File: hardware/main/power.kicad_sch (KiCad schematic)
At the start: 0 parts

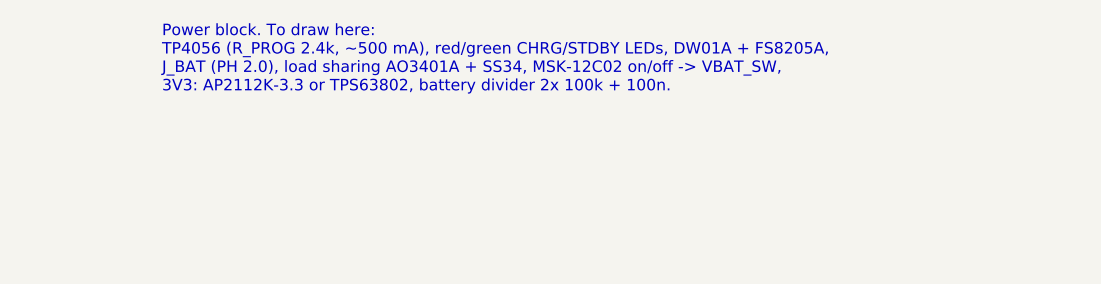
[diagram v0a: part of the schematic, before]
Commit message: hardware: footprints for every part, LCSC library, real A1S pin plan
- lib/lcsc: ESP32-A1S, NS4150B, FS8205A, MSK12C02, PJ-320D imported
  from LCSC with easyeda2kicad (3D paths fixed, NPTH pegs, A1S antenna
  keepout and courtyard), registered in all three projects.
- Parts table with footprint and LCSC number in hardware/README.md.
- The A1S keeps the codec's I2C/I2S inside: display moves to the
  ST7789's pins 14/13/15/22 (SPI or I2C), LED to 12, CHRG/STDBY to 4/2
  through BAT54W. J_SW and J_CHG for an off-board switch and charge LEDs.
- Block sheets use the module's real outputs (HPOUTL/R, SPOLP/N, SPORP/N).

Co-Authored-By: Claude Opus 5.5 <noreply@anthropic.com>
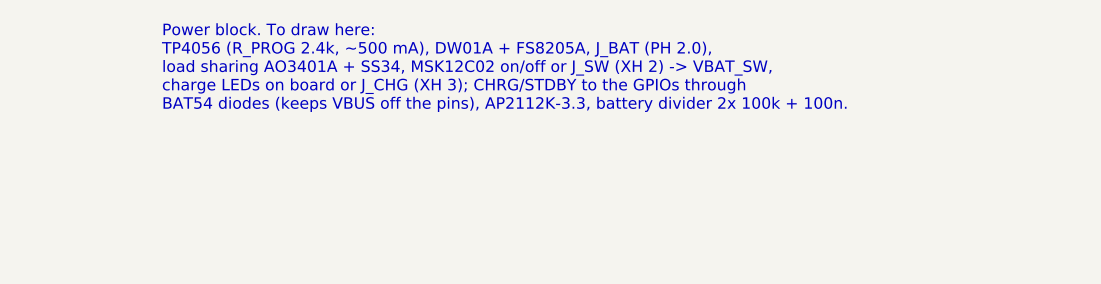
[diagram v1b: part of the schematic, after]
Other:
- note added: "Power block. To draw here: TP4056 (R_PROG 2.4k, ~500 mA), DW01A + FS8205A, J_BAT (PH 2.0), load sharing AO3401A + SS34, MSK12C02 on/off or J_SW (XH 2) -> VBAT_SW, charge LEDs on board or J_CHG (XH 3); CHRG/STDBY to the GPIOs through BAT54 diodes (keeps VBUS off the pins), AP2112K-3.3, battery divider 2x 100k + 100n."
- note removed: "Power block. To draw here: TP4056 (R_PROG 2.4k, ~500 mA), red/green CHRG/STDBY LEDs, DW01A + FS8205A, J_BAT (PH 2.0), load sharing AO3401A + SS34, MSK-12C02 on/off -> VBAT_SW, 3V3: AP2112K-3.3 or TPS63802, battery divider 2x 100k + 100n."
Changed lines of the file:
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@@
 		(rev "A")
 	)
-	(text "Power block. To draw here:\nTP4056 (R_PROG 2.4k, ~500 mA), red/green CHRG/STDBY LEDs, DW01A + FS8205A,\nJ_BAT (PH 2.0), load sharing AO3401A + SS34, MSK-12C02 on/off -> VBAT_SW,\n3V3: AP2112K-3.3 or TPS63802, battery divider 2x 100k + 100n."
+	(text "Power block. To draw here:\nTP4056 (R_PROG 2.4k, ~500 mA), DW01A + FS8205A, J_BAT (PH 2.0),\nload sharing AO3401A + SS34, MSK12C02 on/off or J_SW (XH 2) -> VBAT_SW,\ncharge LEDs on board or J_CHG (XH 3); CHRG/STDBY to the GPIOs through\nBAT54 diodes (keeps VBUS off the pins), AP2112K-3.3, battery divider 2x 100k + 100n."
 		(exclude_from_sim no)
 		(at 101.6 40.64 0)
@@
 		)
 	)
-	(hierarchical_label "CHRG"
+	(hierarchical_label "STDBY"
 		(shape output)
-		(at 50.8 55.88 180)
+		(at 50.8 60.96 180)
+		(effects
+			(font
+				(size 1.27 1.27)
+			)
+			(justify right)
+		)
+	)
+	(hierarchical_label "VBAT_SENSE"
+		(shape output)
+		(at 50.8 66.04 180)
 		(effects
 			(font
@@
 		)
 	)
-	(hierarchical_label "STDBY"
+	(hierarchical_label "CHRG"
 		(shape output)
-		(at 50.8 60.96 180)
+		(at 50.8 55.88 180)
 		(effects
 			(font
-				(size 1.27 1.27)
-			)
-			(justify right)
-		)
-	)
-	(hierarchical_label "VBAT_SENSE"
-		(shape output)
-		(at 50.8 66.04 180)
-		(effects
-			(font

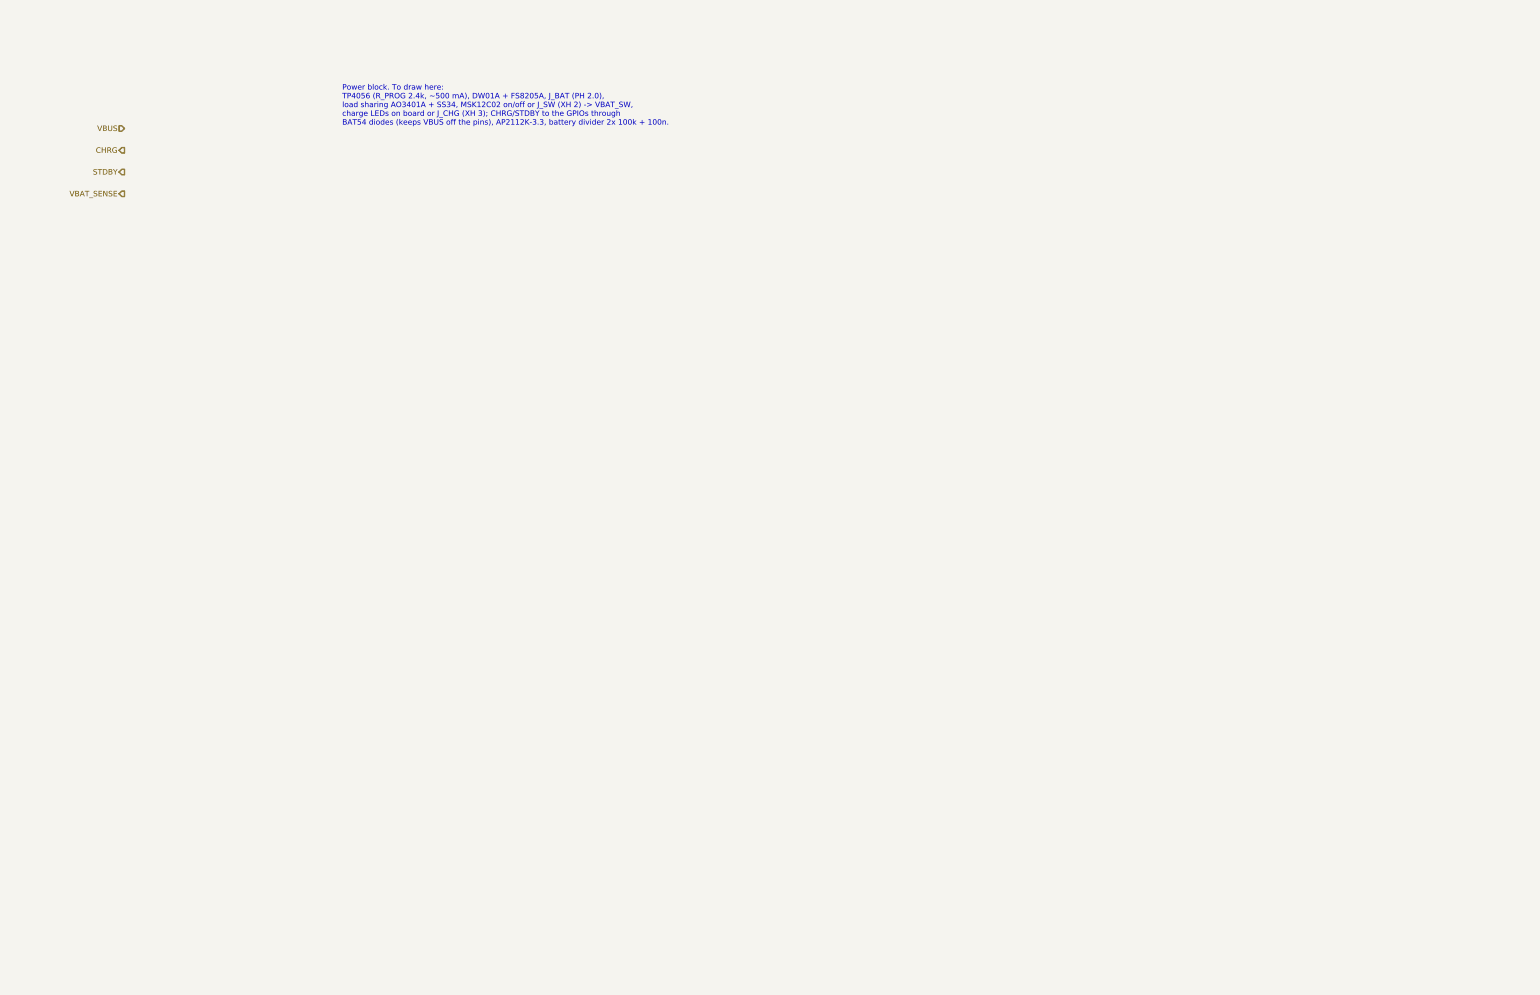
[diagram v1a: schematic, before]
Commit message: hardware: Power sheet (charger, protection, load sharing, switch, 3V3, battery sense)
Co-Authored-By: Claude Opus 5.5 <noreply@anthropic.com>
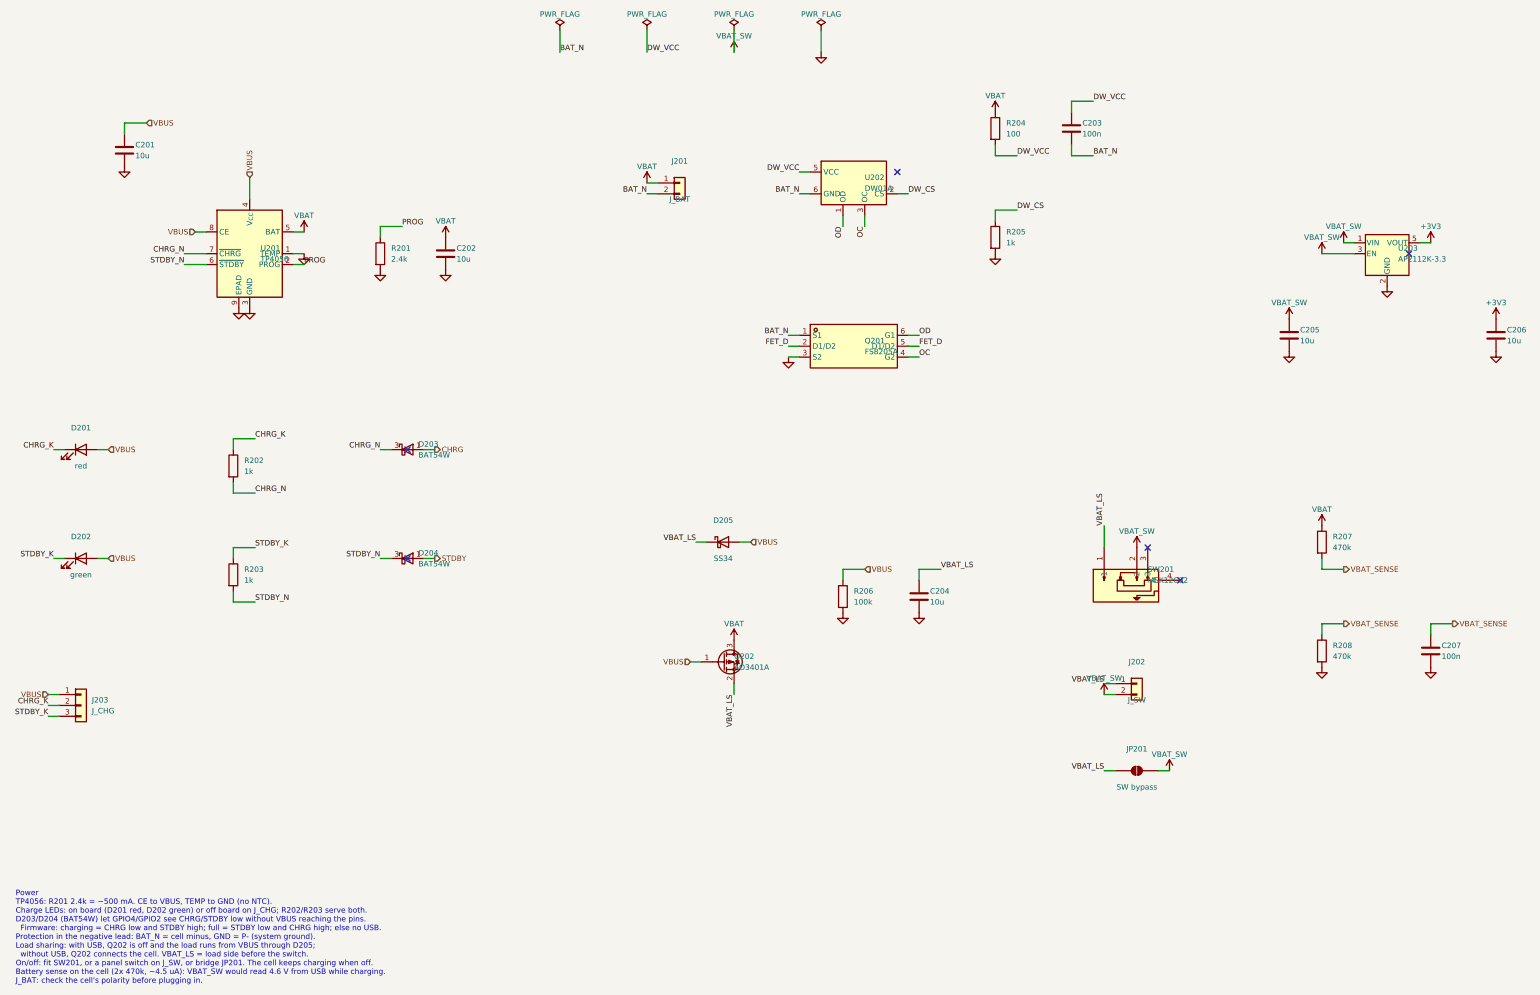
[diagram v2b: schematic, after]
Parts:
- added C201, C202, C204, C205, C206: 10u, Capacitor_SMD:C_0805_2012Metric, symbol Device:C
- added C203, C207: 100n, Capacitor_SMD:C_0805_2012Metric, symbol Device:C
- added D201: red, LED_SMD:LED_0805_2012Metric, symbol Device:LED
- added D202: green, LED_SMD:LED_0805_2012Metric, symbol Device:LED
- added D203, D204: BAT54W, Package_TO_SOT_SMD:SOT-323_SC-70, symbol Diode:BAT54W
- added D205: SS34, Diode_SMD:D_SMA, symbol Diode:SS34
- added J201: J_BAT, Connector_JST:JST_PH_B2B-PH-K_1x02_P2.00mm_Vertical, symbol Connector_Generic:Conn_01x02
- added J202: J_SW, Connector_JST:JST_XH_B2B-XH-A_1x02_P2.50mm_Vertical, symbol Connector_Generic:Conn_01x02
- added J203: J_CHG, Connector_JST:JST_XH_B3B-XH-A_1x03_P2.50mm_Vertical, symbol Connector_Generic:Conn_01x03
- added JP201: SW bypass, Jumper:SolderJumper-2_P1.3mm_Open_RoundedPad1.0x1.5mm, symbol Jumper:SolderJumper_2_Open
- added Q201: FS8205A, lcsc:SOT-23-6_L2.9-W1.6-P0.95-LS2.8-BR, symbol lcsc:FS8205A_C2830320
- added Q202: AO3401A, Package_TO_SOT_SMD:SOT-23, symbol Transistor_FET:AO3401A
- added R201: 2.4k, Resistor_SMD:R_0805_2012Metric, symbol Device:R
- added R202, R203, R205: 1k, Resistor_SMD:R_0805_2012Metric, symbol Device:R
- added R204: 100, Resistor_SMD:R_0805_2012Metric, symbol Device:R
- added R206: 100k, Resistor_SMD:R_0805_2012Metric, symbol Device:R
- added R207, R208: 470k, Resistor_SMD:R_0805_2012Metric, symbol Device:R
- added SW201: MSK12C02, lcsc:SW-TH_MSK12C02, symbol lcsc:MSK12C02
- added U201: TP4056, Package_SO:SOIC-8-1EP_3.9x4.9mm_P1.27mm_EP2.41x3.3mm_ThermalVias, symbol Battery_Management:TP4056-42-ESOP8
- added U202: DW01A, Package_TO_SOT_SMD:SOT-23-6, symbol Battery_Management:DW01A
- added U203: AP2112K-3.3, Package_TO_SOT_SMD:SOT-23-5, symbol Regulator_Linear:AP2112K-3.3
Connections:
- net CHRG: now also D203.1 (A)
- net STDBY: now also D204.1 (A)
- net VBAT_SENSE: now also C207.1, R207.2, R208.1
- net VBUS: now also C201.1, D201.2 (A), D202.2 (A), D205.2 (A), J203.1 (Pin_1), Q202.1 (G), R206.1, U201.4 (V_{CC}), U201.8 (CE)
- new net +3V3: C206.1, U203.5 (VOUT)
- new net BAT_N: C203.2, J201.2 (Pin_2), Q201.1 (S1), U202.6 (GND)
- new net CHRG_K: D201.1 (K), J203.2 (Pin_2), R202.1
- new net CHRG_N: D203.3 (K), R202.2, U201.7 (~{CHRG})
- new net DW_CS: R205.1, U202.2 (CS)
- new net DW_VCC: C203.1, R204.2, U202.5 (VCC)
- new net FET_D: Q201.2 (D1/D2), Q201.5 (D1/D2)
- new net GND: C201.2, C202.2, C204.2, C205.2, C206.2, C207.2, Q201.3 (S2), R201.2, R205.2, R206.2, R208.2, U201.1 (TEMP), U201.3 (GND), U201.9 (EPAD), U203.2 (GND)
- new net OC: Q201.4 (G2), U202.3 (OC)
- new net OD: Q201.6 (G1), U202.1 (OD)
- new net PROG: R201.1, U201.2 (PROG)
- new net STDBY_K: D202.1 (K), J203.3 (Pin_3), R203.1
- new net STDBY_N: D204.3 (K), R203.2, U201.6 (~{STDBY})
- new net VBAT: C202.1, J201.1 (Pin_1), Q202.3 (D), R204.1, R207.1, U201.5 (BAT)
- new net VBAT_LS: C204.1, D205.1 (K), J202.1 (Pin_1), JP201.1 (A), Q202.2 (S), SW201.1
- new net VBAT_SW: C205.1, J202.2 (Pin_2), JP201.2 (B), SW201.2, U203.1 (VIN), U203.3 (EN)
- no-connect marks 0 -> 6
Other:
- note added: "Power TP4056: R201 2.4k = ~500 mA. CE to VBUS, TEMP to GND (no NTC). Charge LEDs: on board (D201 red, D202 green) or off board on J_CHG; R202/R203 serve both. D203/D204 (BAT54W) let GPIO4/GPIO2 see CHRG/STDBY low without VBUS reaching the pins. Firmware: charging = CHRG low and STDBY high; full = STDBY low and CHRG high; else no USB. Protection in the negative lead: BAT_N = cell minus, GND = P- (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"
- note removed: "Power block. To draw here: TP4056 (R_PROG 2.4k, ~500 mA), DW01A + FS8205A, J_BAT (PH 2.0), load sharing AO3401A + SS34, MSK12C02 on/off or J_SW (XH 2) -> VBAT_SW, charge LEDs on board or J_CHG (XH 3); CHRG/STDBY to the GPIOs through BAT54 diodes (keeps VBUS off the pins), AP2112K-3.3, battery divider 2x 100k + 100n."

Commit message: hardware: tidy the Power sheet layout (netlist unchanged)
Co-Authored-By: Claude Opus 5.5 <noreply@anthropic.com>
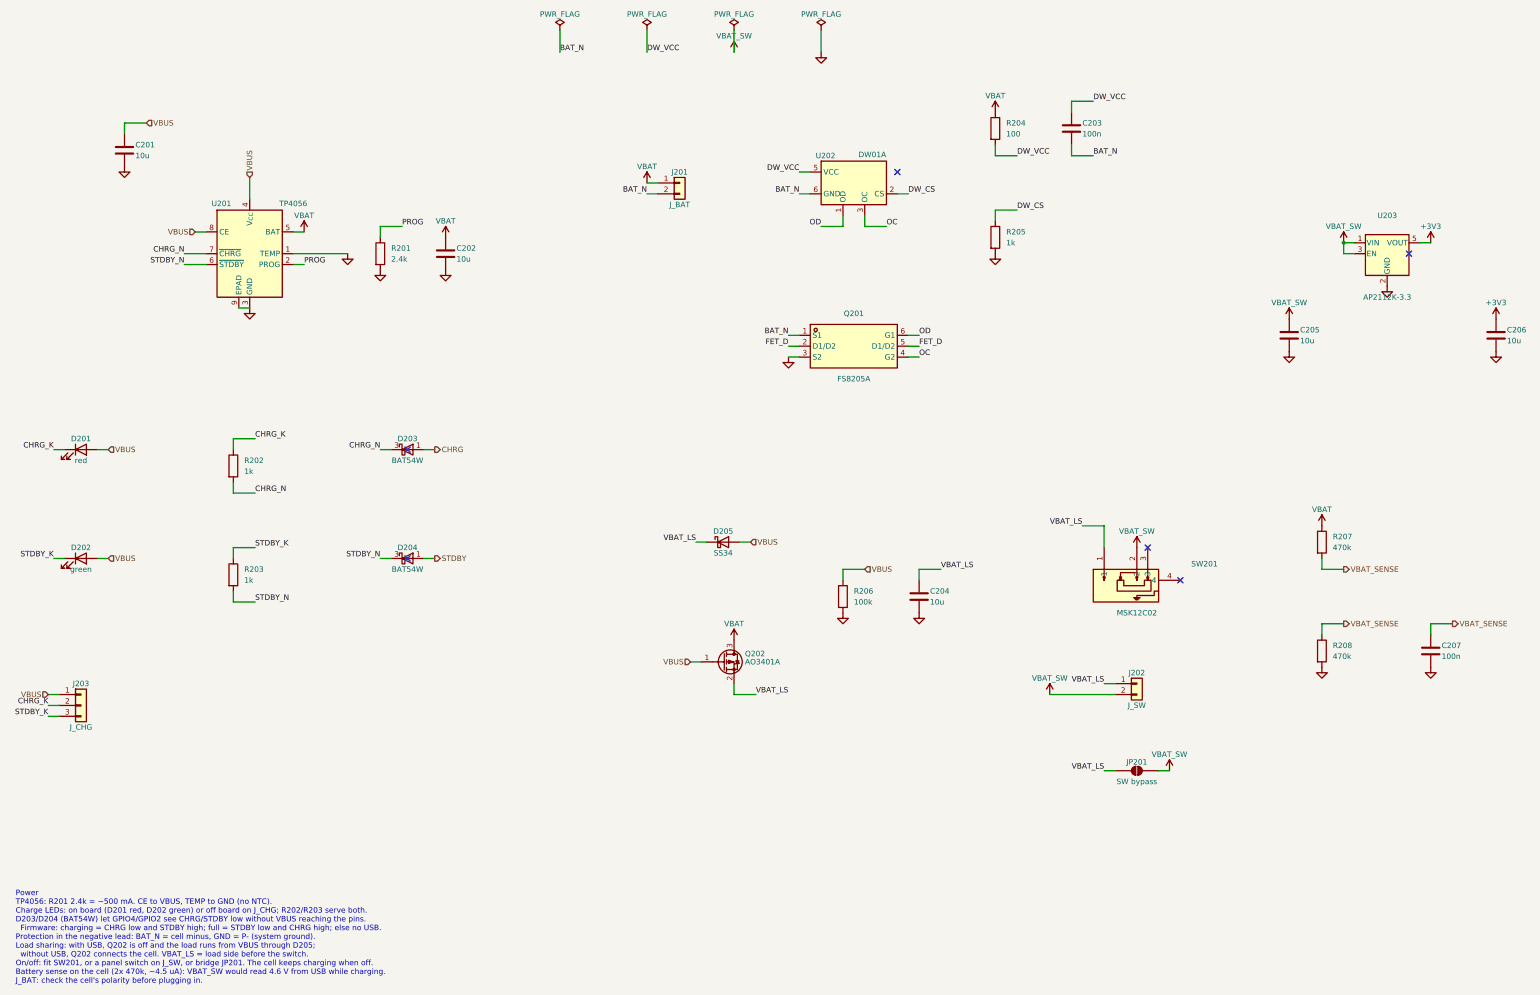
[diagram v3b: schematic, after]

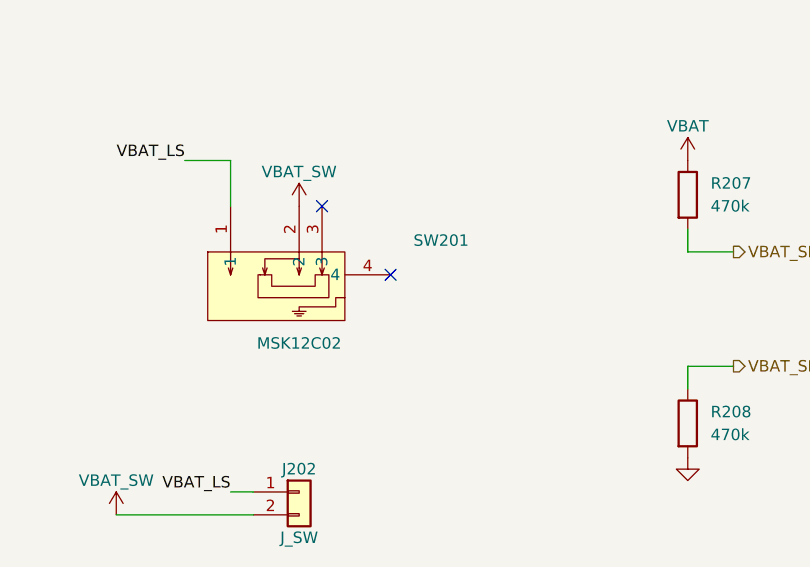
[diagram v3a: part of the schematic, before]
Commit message: hardware: footprints and nets in all three boards, JLC design rules
- Update PCB from Schematic on main, front panel and USB-C board.
- Design rules for JLCPCB 2-layer (0.15 mm track/clearance, 0.3 mm
  drill, 0.6 mm vias, 0.3 mm to the edge); net classes Power (1.0 mm),
  Speaker (0.6 mm), Supply3V3 (0.4 mm).
- TP4056 on the SOIC-8-EP footprint without 0.2 mm thermal vias;
  MSK12C02 footprint marked SMD, its shell pads to GND.
- Generator keeps symbol UUIDs stable so regenerated sheets stay linked.

Co-Authored-By: Claude Opus 5.5 <noreply@anthropic.com>
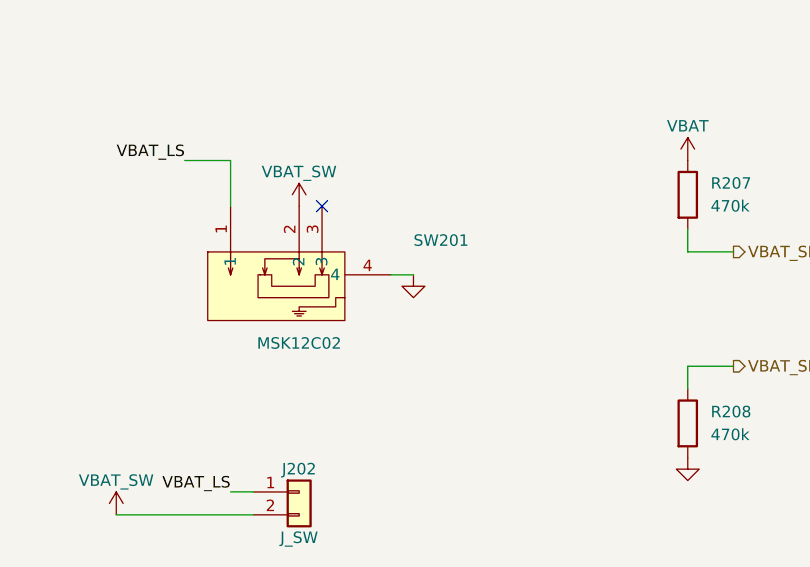
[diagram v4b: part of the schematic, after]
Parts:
- U201: footprint Package_SO:SOIC-8-1EP_3.9x4.9mm_P1.27mm_EP2.41x3.3mm_ThermalVias -> Package_SO:SOIC-8-1EP_3.9x4.9mm_P1.27mm_EP2.41x3.3mm
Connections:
- net GND: now also SW201.4
- no-connect marks 6 -> 5

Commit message: hardware: bare panel/USB-C boards updated, XH battery, holes in, round corners
- Boards updated from the schematics: J_USB XH 6 with CC1/CC2, panel
  without parts (J604 LED header), USB-C board without parts.
- J_BAT JST XH 2.
- M3 holes 4.5 mm in from the edges (heads stay on the board), M2 3 mm;
  rounded corners. DRC: no copper, courtyard or outline errors.

Co-Authored-By: Claude Opus 5.5 <noreply@anthropic.com>
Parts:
- J201: footprint Connector_JST:JST_PH_B2B-PH-K_1x02_P2.00mm_Vertical -> Connector_JST:JST_XH_B2B-XH-A_1x02_P2.50mm_Vertical
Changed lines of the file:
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@@
 			)
 		)
-		(property "Footprint" "Connector_JST:JST_PH_B2B-PH-K_1x02_P2.00mm_Vertical"
+		(property "Footprint" "Connector_JST:JST_XH_B2B-XH-A_1x02_P2.50mm_Vertical"
 			(at 180.34 63.5 0)
 			(hide yes)
